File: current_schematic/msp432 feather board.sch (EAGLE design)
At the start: 53 parts, among them IC1 FT232RL, J1 1981568-1, J2 B2B-PH-SM4-TB(LF)(SN), U1 DMG3415U-7X2-DFN2015-3, U2 MCP73831T-2ACI/OT, X1 TSW-116-07-G-S, X2 TSW-116-07-G-S, Y1 ECS-480-10-37-JTN-TR

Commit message: Add files via upload
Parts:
- C10: value 50nF -> 47nF
- C11: value 5uF -> 4.7uF
- R9: value (none) -> 100K
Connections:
- removed net N$45: C17.1, Y1.IN/OUT
- removed net N$46: C16.1, Y1.OUT/IN
- removed net P4.4: U$1.P4.3/MCLK/RTCCLK/A10, X2-4.1
- new net P4.2: U$1.P4.2/ACLK/TA2CLK/A11, X2-5.1
- net GND: now also C16.2, C17.2
- net N$47: now also C16.1, Y1.OUT/IN; no longer C16.2
- net N$48: now also C17.1, Y1.IN/OUT; no longer C17.2
- net P4.3: now also U$1.P4.3/MCLK/RTCCLK/A10, X2-4.1; no longer U$1.P4.2/ACLK/TA2CLK/A11, X2-5.1
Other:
- note added: "Designed by Seth Kerr 06/21/2020"
- note added: "MSP432P401R Feather Board"
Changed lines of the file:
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@@
 <part name="SUPPLY8" library="supply2" library_urn="urn:adsk.eagle:library:372" deviceset="VCC" device="" value="+3.3V"/>
 <part name="C9" library="rcl" library_urn="urn:adsk.eagle:library:334" deviceset="C-US" device="C0402" package3d_urn="urn:adsk.eagle:package:23626/2" value="0.1uF"/>
-<part name="C10" library="rcl" library_urn="urn:adsk.eagle:library:334" deviceset="C-US" device="C0402" package3d_urn="urn:adsk.eagle:package:23626/2" value="50nF"/>
-<part name="C11" library="rcl" library_urn="urn:adsk.eagle:library:334" deviceset="C-US" device="C0603" package3d_urn="urn:adsk.eagle:package:23616/2" value="5uF"/>
+<part name="C10" library="rcl" library_urn="urn:adsk.eagle:library:334" deviceset="C-US" device="C0402" package3d_urn="urn:adsk.eagle:package:23626/2" value="47nF"/>
+<part name="C11" library="rcl" library_urn="urn:adsk.eagle:library:334" deviceset="C-US" device="C0603" package3d_urn="urn:adsk.eagle:package:23616/2" value="4.7uF"/>
 <part name="SUPPLY13" library="supply2" library_urn="urn:adsk.eagle:library:372" deviceset="VCC" device="" value="+3.3V"/>
 <part name="SUPPLY3" library="supply2" library_urn="urn:adsk.eagle:library:372" deviceset="VCC" device="" value="+3.3V"/>
@@
 <part name="SUPPLY30" library="supply2" library_urn="urn:adsk.eagle:library:372" deviceset="GND" device=""/>
 <part name="U$4" library="MBR0520LT1G" deviceset="MBR0520LT1G" device=""/>
-<part name="R9" library="rcl" library_urn="urn:adsk.eagle:library:334" deviceset="R-US_" device="R0402" package3d_urn="urn:adsk.eagle:package:23547/3"/>
+<part name="R9" library="rcl" library_urn="urn:adsk.eagle:library:334" deviceset="R-US_" device="R0402" package3d_urn="urn:adsk.eagle:package:23547/3" value="100K"/>
 <part name="U2" library="MCP73831-2ACI" deviceset="MCP73831T-2ACI/OT" device=""/>
 <part name="R10" library="rcl" library_urn="urn:adsk.eagle:library:334" deviceset="R-US_" device="R0402" package3d_urn="urn:adsk.eagle:package:23547/3" value="2K2"/>
@@
 <wire x1="210.82" y1="-101.6" x2="210.82" y2="195.58" width="0.1524" layer="94"/>
 <wire x1="210.82" y1="195.58" x2="-172.72" y2="195.58" width="0.1524" layer="94"/>
+<text x="-165.1" y="-96.52" size="5.08" layer="95">Designed by Seth Kerr
+06/21/2020</text>
+<text x="-167.64" y="185.42" size="5.08" layer="95">MSP432P401R Feather Board</text>
 </plain>
 <instances>
@@
 <label x="-25.4" y="-66.04" size="1.778" layer="95" rot="R180" xref="yes"/>
 </segment>
+<segment>
+<pinref part="C17" gate="G$1" pin="2"/>
+<wire x1="-73.66" y1="177.8" x2="-76.2" y2="177.8" width="0.1524" layer="91"/>
+<label x="-76.2" y="177.8" size="1.778" layer="95" rot="R180" xref="yes"/>
+</segment>
+<segment>
+<pinref part="C16" gate="G$1" pin="2"/>
+<wire x1="-12.7" y1="177.8" x2="-12.7" y2="172.72" width="0.1524" layer="91"/>
+<label x="-12.7" y="172.72" size="1.778" layer="95" rot="R270" xref="yes"/>
+</segment>
 </net>
 <net name="+3.3V" class="1">
@@
 </segment>
 </net>
-<net name="N$45" class="0">
-<segment>
-<pinref part="C17" gate="G$1" pin="1"/>
-<wire x1="-60.96" y1="177.8" x2="-66.04" y2="177.8" width="0.1524" layer="91"/>
-<pinref part="Y1" gate="G$1" pin="IN/OUT"/>
-</segment>
-</net>
-<net name="N$46" class="0">
-<segment>
+<net name="N$47" class="0">
+<segment>
+<pinref part="U$1" gate="G$1" pin="PJ.2/HFXOUT"/>
+<wire x1="-30.48" y1="154.94" x2="-30.48" y2="121.92" width="0.1524" layer="91"/>
+<wire x1="-30.48" y1="121.92" x2="-33.02" y2="121.92" width="0.1524" layer="91"/>
 <pinref part="C16" gate="G$1" pin="1"/>
 <wire x1="-20.32" y1="177.8" x2="-25.4" y2="177.8" width="0.1524" layer="91"/>
 <pinref part="Y1" gate="G$1" pin="OUT/IN"/>
-</segment>
-</net>
-<net name="N$47" class="0">
-<segment>
-<pinref part="C16" gate="G$1" pin="2"/>
-<wire x1="-12.7" y1="177.8" x2="-30.48" y2="154.94" width="0.1524" layer="91"/>
-<pinref part="U$1" gate="G$1" pin="PJ.2/HFXOUT"/>
-<wire x1="-30.48" y1="154.94" x2="-30.48" y2="121.92" width="0.1524" layer="91"/>
-<wire x1="-30.48" y1="121.92" x2="-33.02" y2="121.92" width="0.1524" layer="91"/>
+<wire x1="-30.48" y1="154.94" x2="-25.4" y2="154.94" width="0.1524" layer="91"/>
+<wire x1="-25.4" y1="154.94" x2="-25.4" y2="177.8" width="0.1524" layer="91"/>
+<junction x="-25.4" y="177.8"/>
 </segment>
 </net>
@@
 <pinref part="U$1" gate="G$1" pin="PJ.3/HFXIN"/>
 <wire x1="-38.1" y1="121.92" x2="-38.1" y2="124.46" width="0.1524" layer="91"/>
-<pinref part="C17" gate="G$1" pin="2"/>
-<wire x1="-38.1" y1="124.46" x2="-58.42" y2="124.46" width="0.1524" layer="91"/>
-<wire x1="-58.42" y1="124.46" x2="-73.66" y2="177.8" width="0.1524" layer="91"/>
+<wire x1="-38.1" y1="124.46" x2="-63.5" y2="124.46" width="0.1524" layer="91"/>
+<pinref part="C17" gate="G$1" pin="1"/>
+<wire x1="-60.96" y1="177.8" x2="-63.5" y2="177.8" width="0.1524" layer="91"/>
+<pinref part="Y1" gate="G$1" pin="IN/OUT"/>
+<wire x1="-63.5" y1="177.8" x2="-66.04" y2="177.8" width="0.1524" layer="91"/>
+<wire x1="-63.5" y1="124.46" x2="-63.5" y2="177.8" width="0.1524" layer="91"/>
+<junction x="-63.5" y="177.8"/>
 </segment>
 </net>
@@
 </segment>
 </net>
-<net name="P4.4" class="0">
+<net name="P4.2" class="0">
+<segment>
+<pinref part="U$1" gate="G$1" pin="P4.2/ACLK/TA2CLK/A11"/>
+<wire x1="30.48" y1="10.16" x2="35.56" y2="10.16" width="0.1524" layer="91"/>
+<label x="35.56" y="10.16" size="1.778" layer="95" xref="yes"/>
+</segment>
+<segment>
+<pinref part="X2" gate="-5" pin="1"/>
+<wire x1="-68.58" y1="-59.69" x2="-68.58" y2="-58.42" width="0.1524" layer="91"/>
+<label x="-68.58" y="-58.42" size="1.778" layer="95" rot="R90"/>
+</segment>
+</net>
+<net name="P4.3" class="0">
+<segment>
+<pinref part="X2" gate="-4" pin="1"/>
+<wire x1="-66.04" y1="-59.69" x2="-66.04" y2="-58.42" width="0.1524" layer="91"/>
+<label x="-66.04" y="-58.42" size="1.778" layer="95" rot="R90"/>
+</segment>
 <segment>
 <pinref part="U$1" gate="G$1" pin="P4.3/MCLK/RTCCLK/A10"/>
 <wire x1="30.48" y1="15.24" x2="35.56" y2="15.24" width="0.1524" layer="91"/>
 <label x="35.56" y="15.24" size="1.778" layer="95" xref="yes"/>
-</segment>
-<segment>
-<pinref part="X2" gate="-4" pin="1"/>
-<wire x1="-66.04" y1="-59.69" x2="-66.04" y2="-58.42" width="0.1524" layer="91"/>
-<label x="-66.04" y="-58.42" size="1.778" layer="95" rot="R90"/>
-</segment>
-</net>
-<net name="P4.3" class="0">
-<segment>
-<pinref part="U$1" gate="G$1" pin="P4.2/ACLK/TA2CLK/A11"/>
-<wire x1="30.48" y1="10.16" x2="35.56" y2="10.16" width="0.1524" layer="91"/>
-<label x="35.56" y="10.16" size="1.778" layer="95" xref="yes"/>
-</segment>
-<segment>
-<pinref part="X2" gate="-5" pin="1"/>
-<wire x1="-68.58" y1="-59.69" x2="-68.58" y2="-58.42" width="0.1524" layer="91"/>
-<label x="-68.58" y="-58.42" size="1.778" layer="95" rot="R90"/>
 </segment>
 </net>
@@
 </drawing>
 <compatibility>
+<note version="6.3" minversion="6.2.2" severity="warning">
+Since Version 6.2.2 text objects can contain more than one line,
+which will not be processed correctly with this version.
+</note>
 <note version="8.2" severity="warning">
 Since Version 8.2, EAGLE supports online libraries. The ids

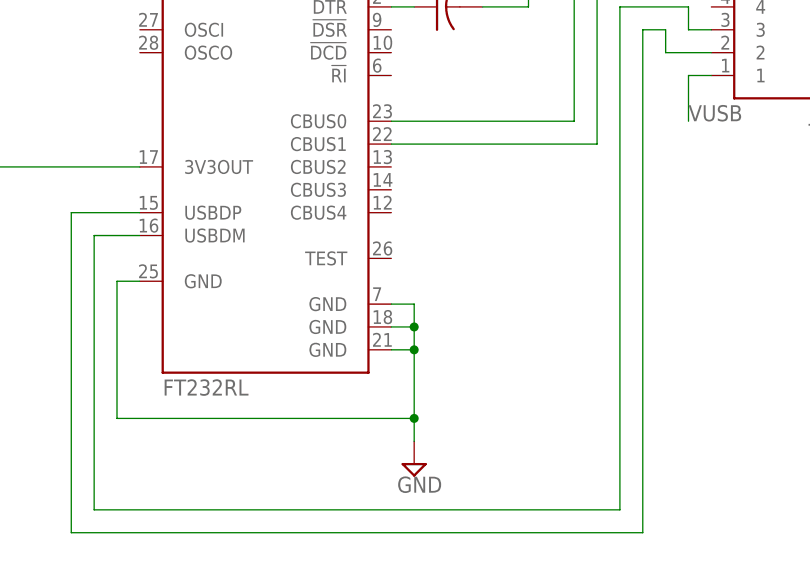
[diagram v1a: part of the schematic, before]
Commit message: updating schematic
Fixed issue with floating TEST pin on FT232RL IC
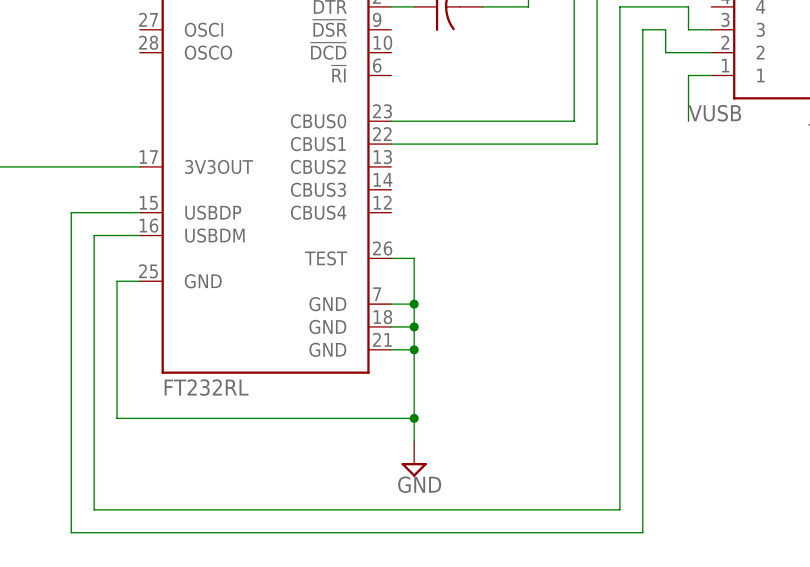
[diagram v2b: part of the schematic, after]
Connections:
- net GND: now also IC1.TEST
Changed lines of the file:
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@@
 <wire x1="106.68" y1="22.86" x2="139.7" y2="22.86" width="0.1524" layer="91"/>
 <junction x="139.7" y="22.86"/>
+<pinref part="IC1" gate="1" pin="TEST"/>
+<wire x1="137.16" y1="40.64" x2="139.7" y2="40.64" width="0.1524" layer="91"/>
+<wire x1="139.7" y1="40.64" x2="139.7" y2="35.56" width="0.1524" layer="91"/>
+<junction x="139.7" y="35.56"/>
 </segment>
 <segment>

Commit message: Add files via upload
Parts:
- removed P2.3_R: (no value), led:LEDCHIP-LED0603
- added J3: (no value), SparkFun-Connectors:CONN_041X04_NO_SILK
- added P2.3/R: (no value), led:LEDCHIP-LED0603
- IC1: device ftdichip:FT232RL -> FT232RL:FT232RL
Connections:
- net N$5 renamed DM
- net N$6 renamed DP
- new net TCK: J3.2, U$1.SWCLKTCK
- new net TDI: J3.3, U$1.PJ.4/TDI
- new net TDO: J3.4, U$1.PJ.5/TDO/SWO
- new net TMS: J3.1, U$1.SWDIOTMS
- net 5V+: no longer IC1.VCC
- net GND: now also IC1.AGND, IC1.GND@18, IC1.GND@21, IC1.GND@7, P2.3/R.C; no longer IC1.GND, IC1.GND@1, IC1.GND@2, IC1.GND@A, P2.3_R.C
- net N$11: now also IC1.!RXLED; no longer IC1.CBUS0
- net N$12: now also IC1.!TXLED; no longer IC1.CBUS1
- net N$3: now also IC1.!RTS; no longer IC1.!DTR
- net N$42: now also P2.3/R.A; no longer P2.3_R.A
- net N$7: now also IC1.RXD; no longer IC1.TXD
- net N$8: now also IC1.TXD; no longer IC1.RXD
- net VIN: now also IC1.VCC
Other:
- moved on the sheet: C1, C10, C11, C12, C16, C17, C2, C3, C4, C5, C6, C7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

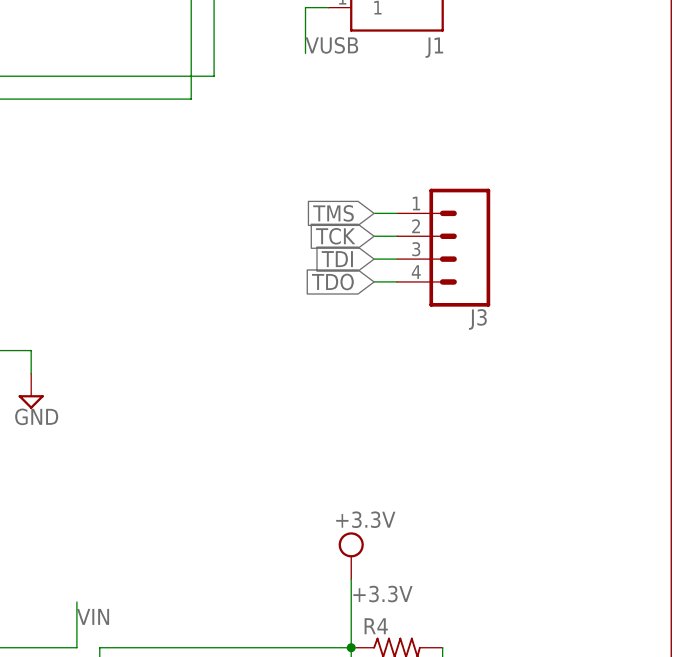
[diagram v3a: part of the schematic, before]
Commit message: Add files via upload
fixing JTAG stuff and adding 10 pin ARM JTAG to schematic and board.
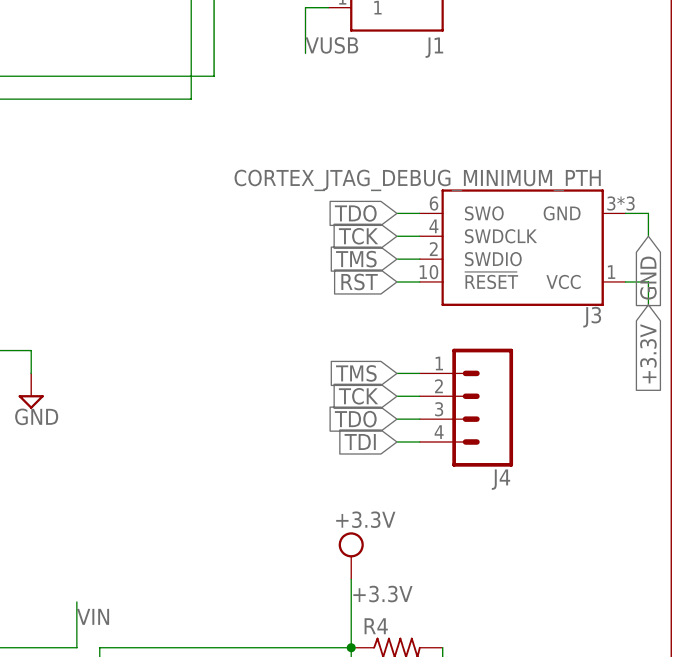
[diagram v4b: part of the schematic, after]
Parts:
- added J4: (no value), SparkFun-Connectors:CONN_041X04_NO_SILK
- J3: value (none) -> CORTEX_JTAG_DEBUG_MINIMUM_PTH; device SparkFun-Connectors:CONN_041X04_NO_SILK -> SparkFun-Connectors:CORTEX_JTAG_DEBUG_MINIMUM_PTH
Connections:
- net +3.3V: now also J3.VCC
- net GND: now also J3.GND
- net RST: now also J3.!RESET
- net TCK: now also J3.SWDCLK, J4.2; no longer J3.2
- net TDI: now also J4.4; no longer J3.3
- net TDO: now also J3.SWO, J4.3; no longer J3.4
- net TMS: now also J3.SWDIO, J4.1; no longer J3.1
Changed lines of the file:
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@@
 <part name="R-NET" library="rcl" library_urn="urn:adsk.eagle:library:334" deviceset="R-US_" device="R0805" package3d_urn="urn:adsk.eagle:package:23553/2" value="0"/>
 <part name="IC1" library="FT232RL" deviceset="FT232RL" device=""/>
-<part name="J3" library="SparkFun-Connectors" deviceset="CONN_04" device="1X04_NO_SILK"/>
+<part name="J3" library="SparkFun-Connectors" deviceset="CORTEX_JTAG_DEBUG_MINIMUM" device="_PTH"/>
+<part name="J4" library="SparkFun-Connectors" deviceset="CONN_04" device="1X04_NO_SILK"/>
 </parts>
 <sheets>
@@
 <attribute name="NAME" x="106.6792" y="38.7335" size="1.5241" layer="95" ratio="10"/>
 </instance>
-<instance part="J3" gate="J1" x="185.42" y="35.56" smashed="yes" rot="R180">
-<attribute name="VALUE" x="190.5" y="42.926" size="1.778" layer="96" font="vector" rot="R180"/>
-<attribute name="NAME" x="190.5" y="27.432" size="1.778" layer="95" font="vector" rot="R180"/>
+<instance part="J3" gate="G$1" x="193.04" y="35.56" smashed="yes" rot="R180">
+<attribute name="NAME" x="203.2" y="27.686" size="1.778" layer="95" font="vector" rot="R180"/>
+<attribute name="VALUE" x="203.2" y="42.926" size="1.778" layer="96" font="vector" rot="R180"/>
+</instance>
+<instance part="J4" gate="J1" x="187.96" y="17.78" smashed="yes" rot="R180">
+<attribute name="VALUE" x="193.04" y="25.146" size="1.778" layer="96" font="vector" rot="R180"/>
+<attribute name="NAME" x="193.04" y="9.652" size="1.778" layer="95" font="vector" rot="R180"/>
 </instance>
 </instances>
@@
 <label x="-25.4" y="172.72" size="1.778" layer="95" rot="R270" xref="yes"/>
 </segment>
+<segment>
+<pinref part="J3" gate="G$1" pin="GND"/>
+<wire x1="205.74" y1="38.1" x2="208.28" y2="38.1" width="0.1524" layer="91"/>
+<wire x1="208.28" y1="38.1" x2="208.28" y2="35.56" width="0.1524" layer="91"/>
+<label x="208.28" y="35.56" size="1.778" layer="95" rot="R270" xref="yes"/>
+</segment>
 </net>
 <net name="+3.3V" class="1">
@@
 <label x="30.48" y="109.22" size="1.778" layer="95"/>
 </segment>
+<segment>
+<pinref part="J3" gate="G$1" pin="VCC"/>
+<wire x1="205.74" y1="30.48" x2="208.28" y2="30.48" width="0.1524" layer="91"/>
+<wire x1="208.28" y1="30.48" x2="208.28" y2="27.94" width="0.1524" layer="91"/>
+<label x="208.28" y="27.94" size="1.778" layer="95" rot="R270" xref="yes"/>
+</segment>
 </net>
 <net name="N$1" class="0">
@@
 <junction x="-35.56" y="152.4"/>
 <label x="-35.56" y="157.48" size="1.778" layer="95"/>
+</segment>
+<segment>
+<wire x1="182.88" y1="30.48" x2="180.34" y2="30.48" width="0.1524" layer="91"/>
+<pinref part="J3" gate="G$1" pin="!RESET"/>
+<label x="180.34" y="30.48" size="1.778" layer="95" rot="R180" xref="yes"/>
 </segment>
 </net>
@@
 <net name="TMS" class="0">
 <segment>
-<pinref part="J3" gate="J1" pin="1"/>
-<wire x1="180.34" y1="38.1" x2="177.8" y2="38.1" width="0.1524" layer="91"/>
-<label x="177.8" y="38.1" size="1.778" layer="95" rot="R180" xref="yes"/>
+<wire x1="182.88" y1="33.02" x2="180.34" y2="33.02" width="0.1524" layer="91"/>
+<label x="180.34" y="33.02" size="1.778" layer="95" rot="R180" xref="yes"/>
+<pinref part="J3" gate="G$1" pin="SWDIO"/>
 </segment>
 <segment>
@@
 <label x="-91.44" y="124.46" size="1.778" layer="95" rot="R90" xref="yes"/>
 </segment>
+<segment>
+<pinref part="J4" gate="J1" pin="1"/>
+<wire x1="182.88" y1="20.32" x2="180.34" y2="20.32" width="0.1524" layer="91"/>
+<label x="180.34" y="20.32" size="1.778" layer="95" rot="R180" xref="yes"/>
+</segment>
 </net>
 <net name="TCK" class="0">
 <segment>
-<pinref part="J3" gate="J1" pin="2"/>
-<wire x1="180.34" y1="35.56" x2="177.8" y2="35.56" width="0.1524" layer="91"/>
-<label x="177.8" y="35.56" size="1.778" layer="95" rot="R180" xref="yes"/>
+<wire x1="182.88" y1="35.56" x2="180.34" y2="35.56" width="0.1524" layer="91"/>
+<label x="180.34" y="35.56" size="1.778" layer="95" rot="R180" xref="yes"/>
+<pinref part="J3" gate="G$1" pin="SWDCLK"/>
 </segment>
 <segment>
@@
 <label x="-96.52" y="124.46" size="1.778" layer="95" rot="R90" xref="yes"/>
 </segment>
+<segment>
+<pinref part="J4" gate="J1" pin="2"/>
+<wire x1="182.88" y1="17.78" x2="180.34" y2="17.78" width="0.1524" layer="91"/>
+<label x="180.34" y="17.78" size="1.778" layer="95" rot="R180" xref="yes"/>
+</segment>
 </net>
 <net name="TDI" class="0">
-<segment>
-<pinref part="J3" gate="J1" pin="3"/>
-<wire x1="180.34" y1="33.02" x2="177.8" y2="33.02" width="0.1524" layer="91"/>
-<label x="177.8" y="33.02" size="1.778" layer="95" rot="R180" xref="yes"/>
-</segment>
 <segment>
 <pinref part="U$1" gate="G$1" pin="PJ.4/TDI"/>
@@
 <label x="-81.28" y="124.46" size="1.778" layer="95" rot="R90" xref="yes"/>
 </segment>
+<segment>
+<pinref part="J4" gate="J1" pin="4"/>
+<wire x1="182.88" y1="12.7" x2="180.34" y2="12.7" width="0.1524" layer="91"/>
+<label x="180.34" y="12.7" size="1.778" layer="95" rot="R180" xref="yes"/>
+</segment>
 </net>
 <net name="TDO" class="0">
 <segment>
-<pinref part="J3" gate="J1" pin="4"/>
-<wire x1="180.34" y1="30.48" x2="177.8" y2="30.48" width="0.1524" layer="91"/>
-<label x="177.8" y="30.48" size="1.778" layer="95" rot="R180" xref="yes"/>
+<wire x1="182.88" y1="38.1" x2="180.34" y2="38.1" width="0.1524" layer="91"/>
+<label x="180.34" y="38.1" size="1.778" layer="95" rot="R180" xref="yes"/>
+<pinref part="J3" gate="G$1" pin="SWO"/>
 </segment>
 <segment>
@@
 <label x="-86.36" y="124.46" size="1.778" layer="95" rot="R90" xref="yes"/>
 </segment>
-</net>
+<segment>
+<pinref part="J4" gate="J1" pin="3"/>
+<wire x1="182.88" y1="15.24" x2="180.34" y2="15.24" width="0.1524" layer="91"/>
+<label x="180.34" y="15.24" size="1.778" layer="95" rot="R180" xref="yes"/>
+</segment>
+</net>

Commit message: Add files via upload
fixed wiring issues on the schematic for the usb interface
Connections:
- net DM: now also J1.2; no longer J1.3
- net DP: now also J1.3; no longer J1.2
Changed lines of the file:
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@@
 </segment>
 <segment>
-<pinref part="J1" gate="G$1" pin="3"/>
-<wire x1="170.18" y1="66.04" x2="172.72" y2="66.04" width="0.1524" layer="91"/>
-<label x="170.18" y="66.04" size="1.778" layer="95" rot="R180" xref="yes"/>
+<pinref part="J1" gate="G$1" pin="2"/>
+<wire x1="167.64" y1="63.5" x2="172.72" y2="63.5" width="0.1524" layer="91"/>
+<label x="167.64" y="63.5" size="1.778" layer="95" rot="R180" xref="yes"/>
 </segment>
 </net>
@@
 </segment>
 <segment>
-<pinref part="J1" gate="G$1" pin="2"/>
-<wire x1="167.64" y1="63.5" x2="172.72" y2="63.5" width="0.1524" layer="91"/>
-<label x="167.64" y="63.5" size="1.778" layer="95" rot="R180" xref="yes"/>
+<pinref part="J1" gate="G$1" pin="3"/>
+<wire x1="170.18" y1="66.04" x2="172.72" y2="66.04" width="0.1524" layer="91"/>
+<label x="170.18" y="66.04" size="1.778" layer="95" rot="R180" xref="yes"/>
 </segment>
 </net>
